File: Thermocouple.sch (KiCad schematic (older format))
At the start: 15 parts

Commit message: 5.3 Video 1/2 Associating and Placing the Relay Module
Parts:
- gave numbers to parts that had none: 13
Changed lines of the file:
@@
 Sheet 7 9
 Title ""
-Date "10 feb 2014"
+Date "19 feb 2014"
 Rev ""
 Comp ""
@@
 CS_N
 $Comp
-L LM324 U?
-U 1 1 52F15A12
+L LM324 U11
+U 2 1 52F15A12
 P 9000 2100
-F 0 "U?" H 9050 2300 60  0000 C CNN
+F 0 "U11" H 9050 2300 60  0000 C CNN
 F 1 "LM324" H 9150 1900 50  0000 C CNN
 F 2 "" H 9000 2100 60  0000 C CNN
 F 3 "" H 9000 2100 60  0000 C CNN
-	1    9000 2100
+	2    9000 2100
 	-1   0    0    -1
 $EndComp
 $Comp
-L LM324 U?
-U 1 1 52F15A1F
+L LM324 U11
+U 3 1 52F15A1F
 P 9000 4000
-F 0 "U?" H 9050 4200 60  0000 C CNN
+F 0 "U11" H 9050 4200 60  0000 C CNN
 F 1 "LM324" H 9150 3800 50  0000 C CNN
 F 2 "" H 9000 4000 60  0000 C CNN
 F 3 "" H 9000 4000 60  0000 C CNN
-	1    9000 4000
+	3    9000 4000
 	-1   0    0    1
 $EndComp
 $Comp
-L LM324 U?
+L LM324 U11
 U 1 1 52F15A25
 P 6700 2950
-F 0 "U?" H 6750 3150 60  0000 C CNN
+F 0 "U11" H 6750 3150 60  0000 C CNN
 F 1 "LM324" H 6850 2750 50  0000 C CNN
 F 2 "" H 6700 2950 60  0000 C CNN
@@
 $EndComp
 $Comp
-L LM324 U?
-U 1 1 52F15A2B
+L LM324 U7
+U 4 1 52F15A2B
 P 5550 5550
-F 0 "U?" H 5600 5750 60  0000 C CNN
+F 0 "U7" H 5600 5750 60  0000 C CNN
 F 1 "LM324" H 5700 5350 50  0000 C CNN
 F 2 "" H 5550 5550 60  0000 C CNN
 F 3 "" H 5550 5550 60  0000 C CNN
-	1    5550 5550
+	4    5550 5550
 	-1   0    0    -1
 $EndComp
 $Comp
-L R R?
+L R R21
 U 1 1 52F15A69
 P 5400 7350
-F 0 "R?" V 5480 7350 40  0000 C CNN
+F 0 "R21" V 5480 7350 40  0000 C CNN
 F 1 "R" V 5407 7351 40  0000 C CNN
 F 2 "" V 5330 7350 30  0000 C CNN
@@
 $EndComp
 $Comp
-L R R?
+L R R26
 U 1 1 52F15A76
 P 8050 2400
-F 0 "R?" V 8130 2400 40  0000 C CNN
+F 0 "R26" V 8130 2400 40  0000 C CNN
 F 1 "R" V 8057 2401 40  0000 C CNN
 F 2 "" V 7980 2400 30  0000 C CNN
@@
 $EndComp
 $Comp
-L R R?
+L R R28
 U 1 1 52F15A7C
 P 8050 3700
-F 0 "R?" V 8130 3700 40  0000 C CNN
+F 0 "R28" V 8130 3700 40  0000 C CNN
 F 1 "R" V 8057 3701 40  0000 C CNN
 F 2 "" V 7980 3700 30  0000 C CNN
@@
 $EndComp
 $Comp
-L R R?
+L R R27
 U 1 1 52F15A8C
 P 8050 3050
-F 0 "R?" V 8130 3050 40  0000 C CNN
+F 0 "R27" V 8130 3050 40  0000 C CNN
 F 1 "R" V 8057 3051 40  0000 C CNN
 F 2 "" V 7980 3050 30  0000 C CNN
@@
 $EndComp
 $Comp
-L R R?
+L R R24
 U 1 1 52F15A92
 P 7600 2100
-F 0 "R?" V 7680 2100 40  0000 C CNN
+F 0 "R24" V 7680 2100 40  0000 C CNN
 F 1 "R" V 7607 2101 40  0000 C CNN
 F 2 "" V 7530 2100 30  0000 C CNN
@@
 $EndComp
 $Comp
-L R R?
+L R R25
 U 1 1 52F15A98
 P 7600 4000
-F 0 "R?" V 7680 4000 40  0000 C CNN
+F 0 "R25" V 7680 4000 40  0000 C CNN
 F 1 "R" V 7607 4001 40  0000 C CNN
 F 2 "" V 7530 4000 30  0000 C CNN
@@
 $EndComp
 $Comp
-L R R?
+L R R22
 U 1 1 52F15B4F
 P 6700 2100
-F 0 "R?" V 6780 2100 40  0000 C CNN
+F 0 "R22" V 6780 2100 40  0000 C CNN
 F 1 "R" V 6707 2101 40  0000 C CNN
 F 2 "" V 6630 2100 30  0000 C CNN
@@
 $EndComp
 $Comp
-L R R?
+L R R23
 U 1 1 52F15B55
 P 6700 4000
-F 0 "R?" V 6780 4000 40  0000 C CNN
+F 0 "R23" V 6780 4000 40  0000 C CNN
 F 1 "R" V 6707 4001 40  0000 C CNN
 F 2 "" V 6630 4000 30  0000 C CNN
@@
 Instrumentation Amp
 $Comp
-L MCP3550-60-E/SN U?
+L MCP3550-60-E/SN U9
 U 1 1 52F18789
 P 3500 3100
-F 0 "U?" H 2950 3450 40  0000 C CNN
+F 0 "U9" H 2950 3450 40  0000 C CNN
 F 1 "MCP3550-60-E/SN" H 3200 3400 40  0000 C CNN
 F 2 "SO8" H 3300 3100 30  0000 C CIN
@@
 	2350 3200 3000 3200
 $Comp
-L +12V #PWR?
+L +12V #PWR039
 U 1 1 52F18A83
 P 9100 1500
-F 0 "#PWR?" H 9100 1450 20  0001 C CNN
+F 0 "#PWR039" H 9100 1450 20  0001 C CNN
 F 1 "+12V" H 9100 1600 30  0000 C CNN
 F 2 "" H 9100 1500 60  0000 C CNN
@@
 	9100 1500 9100 1700
 $Comp
-L +12V #PWR?
+L +12V #PWR040
 U 1 1 52F18AB9
 P 9100 4650
-F 0 "#PWR?" H 9100 4600 20  0001 C CNN
+F 0 "#PWR040" H 9100 4600 20  0001 C CNN
 F 1 "+12V" H 9100 4750 30  0000 C CNN
 F 2 "" H 9100 4650 60  0000 C CNN
@@
 	9100 4400 9100 4650
 $Comp
-L -12V #PWR?
+L -12V #PWR041
 U 1 1 52F18AF7
 P 9100 3500
-F 0 "#PWR?" H 9100 3630 20  0001 C CNN
+F 0 "#PWR041" H 9100 3630 20  0001 C CNN
 F 1 "-12V" H 9100 3600 30  0000 C CNN
 F 2 "" H 9100 3500 60  0000 C CNN
@@
 	9100 3500 9100 3600
 $Comp
-L -12V #PWR?
+L -12V #PWR042
 U 1 1 52F18B36
 P 9100 2600
-F 0 "#PWR?" H 9100 2730 20  0001 C CNN
+F 0 "#PWR042" H 9100 2730 20  0001 C CNN
 F 1 "-12V" H 9100 2700 30  0000 C CNN
 F 2 "" H 9100 2600 60  0000 C CNN
@@
 	9100 2500 9100 2600
 $Comp
-L -12V #PWR?
+L -12V #PWR043
 U 1 1 52F18BB0
 P 6800 2350
-F 0 "#PWR?" H 6800 2480 20  0001 C CNN
+F 0 "#PWR043" H 6800 2480 20  0001 C CNN
 F 1 "-12V" H 6800 2450 30  0000 C CNN
 F 2 "" H 6800 2350 60  0000 C CNN
@@
 $EndComp
 $Comp
-L +12V #PWR?
+L +12V #PWR044
 U 1 1 52F18BB6
 P 6800 3500
-F 0 "#PWR?" H 6800 3450 20  0001 C CNN
+F 0 "#PWR044" H 6800 3450 20  0001 C CNN
 F 1 "+12V" H 6800 3600 30  0000 C CNN
 F 2 "" H 6800 3500 60  0000 C CNN
@@
 	6200 2950 6200 2100
 $Comp
-L GND #PWR?
+L GND #PWR045
 U 1 1 52F18C2C
 P 6200 4200
-F 0 "#PWR?" H 6200 4200 30  0001 C CNN
+F 0 "#PWR045" H 6200 4200 30  0001 C CNN
 F 1 "GND" H 6200 4130 30  0001 C CNN
 F 2 "" H 6200 4200 60  0000 C CNN
@@
 	6200 4000 6200 4200
 $Comp
-L MCP3550-60-E/SN U?
+L MCP3550-60-E/SN U10
 U 1 1 52F18C65
 P 3500 5700
-F 0 "U?" H 2950 6050 40  0000 C CNN
+F 0 "U10" H 2950 6050 40  0000 C CNN
 F 1 "MCP3550-60-E/SN" H 3200 6000 40  0000 C CNN
 F 2 "SO8" H 3300 5700 30  0000 C CIN
@@
 Connection ~ 4850 5550
 $Comp
-L ZENER D?
+L ZENER D5
 U 1 1 52F18D23
 P 7350 5850
-F 0 "D?" H 7350 5950 50  0000 C CNN
+F 0 "D5" H 7350 5950 50  0000 C CNN
 F 1 "ZENER" H 7350 5750 40  0000 C CNN
 F 2 "" H 7350 5850 60  0000 C CNN
@@
 $EndComp
 $Comp
-L +12V #PWR?
+L +12V #PWR046
 U 1 1 52F18D32
 P 7350 5250
-F 0 "#PWR?" H 7350 5200 20  0001 C CNN
+F 0 "#PWR046" H 7350 5200 20  0001 C CNN
 F 1 "+12V" H 7350 5350 30  0000 C CNN
 F 2 "" H 7350 5250 60  0000 C CNN
@@
 	7350 5250 7350 5650
 $Comp
-L AGND #PWR?
+L AGND #PWR047
 U 1 1 52F18D78
 P 7350 6450
-F 0 "#PWR?" H 7350 6450 40  0001 C CNN
+F 0 "#PWR047" H 7350 6450 40  0001 C CNN
 F 1 "AGND" H 7350 6380 50  0000 C CNN
 F 2 "" H 7350 6450 60  0000 C CNN

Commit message: 5.4 Video 1/2 Associating and Placing the Thermocouple Module
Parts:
- removed D5: ZENER, symbol ZENER
- removed R21: R, symbol R
- removed U10, U9: MCP3550-60-E/SN, SO8, symbol MCP3550-60-E/SN
- removed U7: LM324, symbol LM324
- added C10, C5, C6, C7, C8, C9: C, ~, symbol C
- added P2: CONN_2, symbol CONN_2
- added P3: CONN_3X2, symbol CONN_3X2
- added R45, R46: R, symbol R
- added U10: MCP3901, symbol MCP3901
- added U11: LMT84, symbol LMT84
- U4: renamed from U11; value LM324 -> OPA4170
- renumbered R23 to R38, R22 to R39, R24 to R40, R25 to R41, R26 to R42, R28 to R43, R27 to R44
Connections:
- net labels added: +5V, REF+, REF-, ~CS, ~DR, ~RESET
- net labels removed: CS_N
- wire segments 39 -> 84
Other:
- note added: "16-24 bit ADC"
- note added: "Analog/TC Input"
- note removed: "16-24 bit ADC, TBD"
- note removed: "Fake Thermocouple"
- note removed: "Unused pins (at this time)\n"
- moved on the sheet: R38, R44

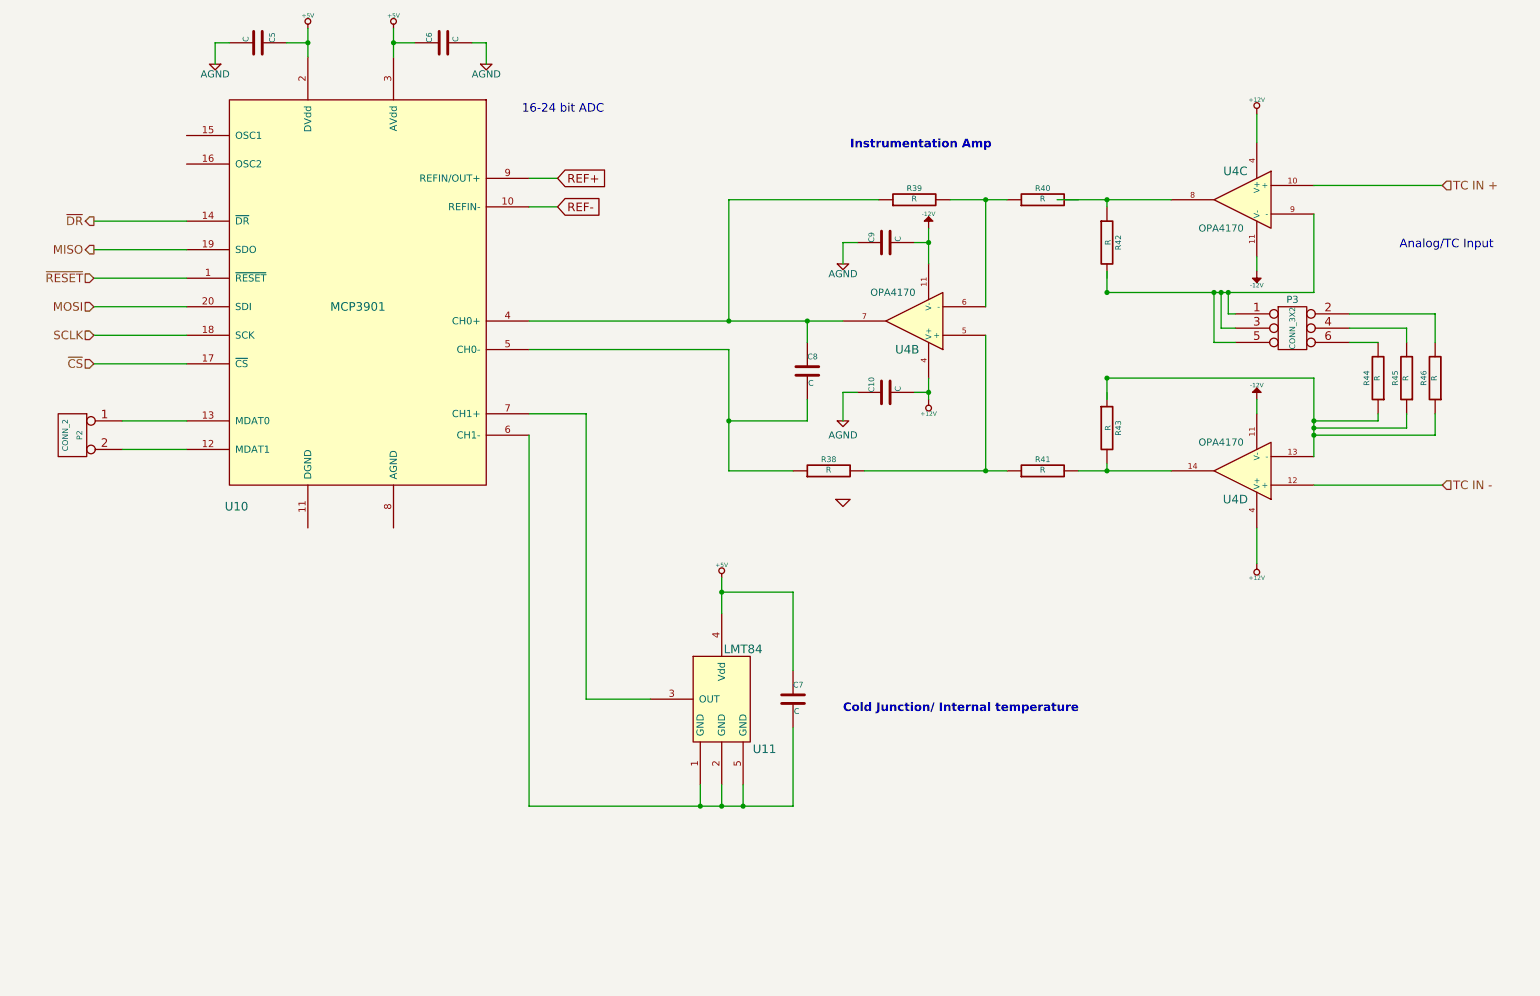
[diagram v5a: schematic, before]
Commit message: 5.4 Video 2/2 Associating and Placing the Thermocouple Module
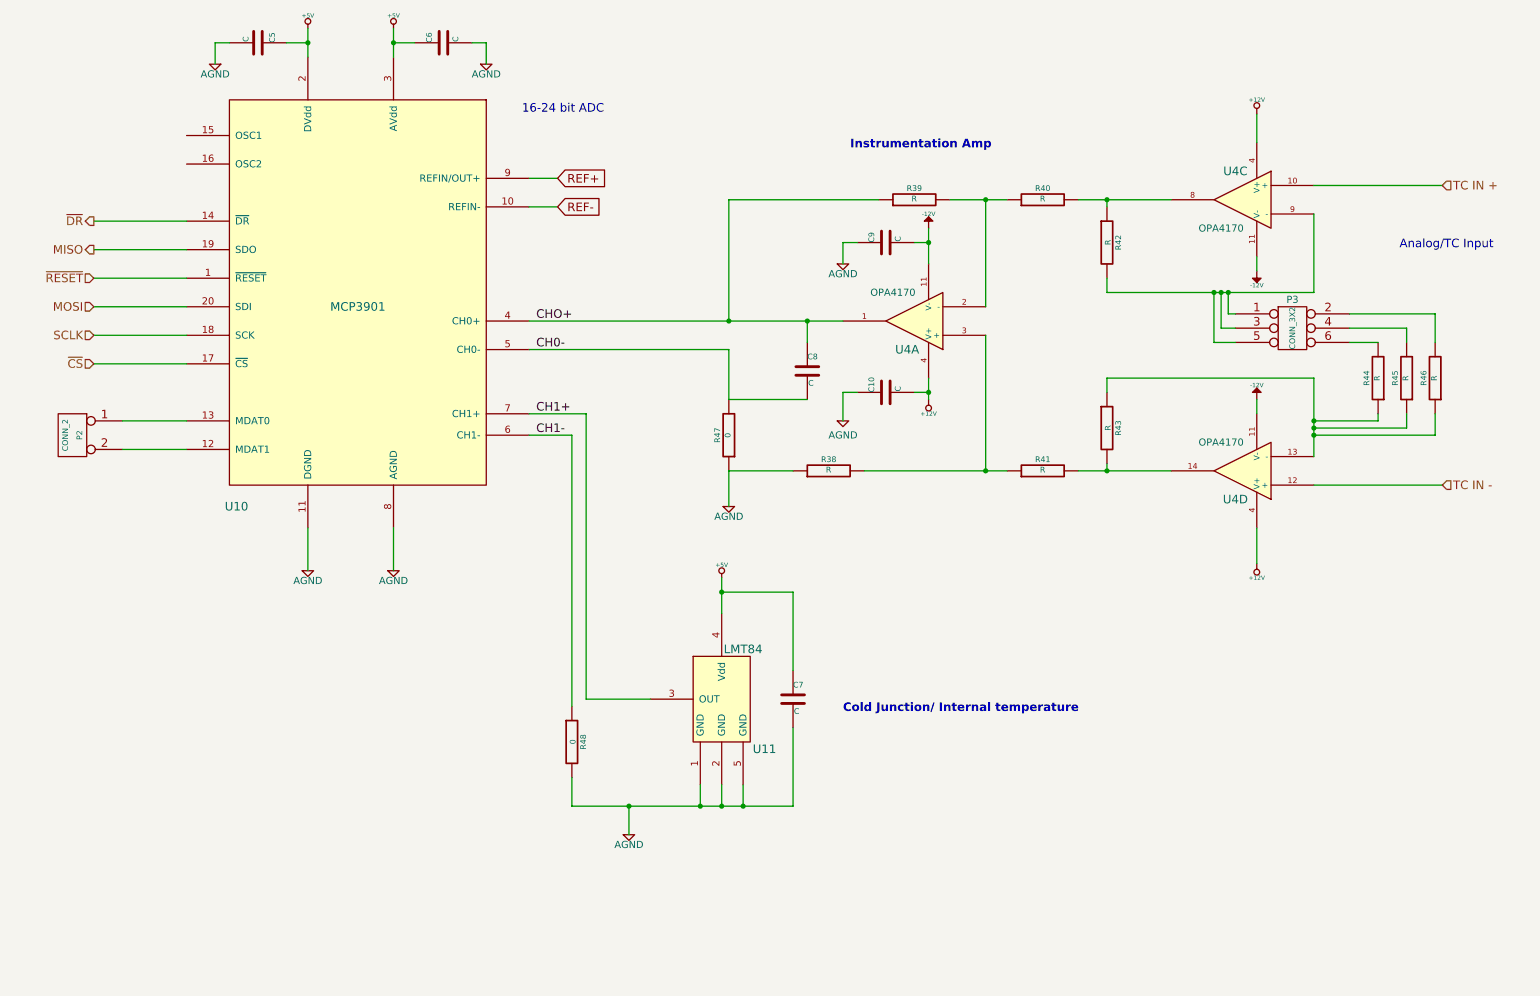
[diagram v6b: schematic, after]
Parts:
- added R47, R48: 0, symbol R
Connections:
- net labels added: CH0-, CH1+, CH1-, CHO+
- net labels removed: GND
- wire segments 84 -> 89
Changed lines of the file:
@@
 LIBS:BenchBudEE
 LIBS:BenchBudEE-cache
-EELAYER 27 0
+EELAYER 24 0
 EELAYER END
 $Descr A4 11693 8268
@@
 $Comp
 L LM324 U4
-U 2 1 52F15A25
+U 1 1 52F15A25
 P 6700 2950
 F 0 "U4" H 6750 3150 60  0000 C CNN
@@
 F 2 "" H 6700 2950 60  0000 C CNN
 F 3 "" H 6700 2950 60  0000 C CNN
-	2    6700 2950
+	1    6700 2950
 	-1   0    0    1
 $EndComp
@@
 	9500 4100 10400 4100
 Wire Wire Line
-	7700 2100 8500 2100
-Connection ~ 8050 2100
-Wire Wire Line
-	8050 2600 8050 2750
-Wire Wire Line
-	8050 3350 8050 3500
+	7850 2100 8500 2100
 Wire Wire Line
 	7850 4000 8500 4000
@@
 Wire Wire Line
 	9500 3350 8050 3350
-Connection ~ 8050 3350
 Wire Wire Line
 	7200 2100 7200 2850
@@
 Instrumentation Amp
 $Comp
-L +12V #PWR52
+L +12V #PWR041
 U 1 1 52F18A83
 P 9100 1500
-F 0 "#PWR52" H 9100 1450 20  0001 C CNN
+F 0 "#PWR041" H 9100 1450 20  0001 C CNN
 F 1 "+12V" H 9100 1600 30  0000 C CNN
 F 2 "" H 9100 1500 60  0000 C CNN
@@
 	9100 1500 9100 1700
 $Comp
-L +12V #PWR55
+L +12V #PWR042
 U 1 1 52F18AB9
 P 9100 4650
-F 0 "#PWR55" H 9100 4600 20  0001 C CNN
+F 0 "#PWR042" H 9100 4600 20  0001 C CNN
 F 1 "+12V" H 9100 4750 30  0000 C CNN
 F 2 "" H 9100 4650 60  0000 C CNN
@@
 	9100 4400 9100 4650
 $Comp
-L -12V #PWR54
+L -12V #PWR043
 U 1 1 52F18AF7
 P 9100 3500
-F 0 "#PWR54" H 9100 3630 20  0001 C CNN
+F 0 "#PWR043" H 9100 3630 20  0001 C CNN
 F 1 "-12V" H 9100 3600 30  0000 C CNN
 F 2 "" H 9100 3500 60  0000 C CNN
@@
 	9100 3500 9100 3600
 $Comp
-L -12V #PWR53
+L -12V #PWR044
 U 1 1 52F18B36
 P 9100 2600
-F 0 "#PWR53" H 9100 2730 20  0001 C CNN
+F 0 "#PWR044" H 9100 2730 20  0001 C CNN
 F 1 "-12V" H 9100 2700 30  0000 C CNN
 F 2 "" H 9100 2600 60  0000 C CNN
@@
 Wire Wire Line
 	8050 2750 9500 2750
-Connection ~ 8050 2750
 Wire Wire Line
 	9100 2500 9100 2600
 $Comp
-L -12V #PWR50
+L -12V #PWR045
 U 1 1 52F18BB0
 P 6800 2300
-F 0 "#PWR50" H 6800 2430 20  0001 C CNN
+F 0 "#PWR045" H 6800 2430 20  0001 C CNN
 F 1 "-12V" H 6800 2400 30  0000 C CNN
 F 2 "" H 6800 2300 60  0000 C CNN
@@
 $EndComp
 $Comp
-L +12V #PWR51
+L +12V #PWR046
 U 1 1 52F18BB6
 P 6800 3500
-F 0 "#PWR51" H 6800 3450 20  0001 C CNN
+F 0 "#PWR046" H 6800 3450 20  0001 C CNN
 F 1 "+12V" H 6800 3600 30  0000 C CNN
 F 2 "" H 6800 3500 60  0000 C CNN
@@
 Wire Wire Line
 	6800 2300 6800 2550
-$Comp
-L GND #PWR49
-U 1 1 52F18C2C
-P 6200 4200
-F 0 "#PWR49" H 6200 4200 30  0001 C CNN
-F 1 "GND" H 6200 4130 30  0001 C CNN
-F 2 "" H 6200 4200 60  0000 C CNN
-F 3 "" H 6200 4200 60  0000 C CNN
-	1    6200 4200
-	1    0    0    -1
-$EndComp
 Text Notes 6200 5700 0    60   ~ 12
 Cold Junction/ Internal temperature
@@
 Wire Wire Line
 	4000 3150 5400 3150
-Wire Wire Line
-	5400 3150 5400 4000
 Connection ~ 5400 2950
 $Comp
@@
 	5950 2950 5950 3100
 Connection ~ 5950 2950
-Wire Wire Line
-	5950 3500 5950 3650
-Wire Wire Line
-	5950 3650 5400 3650
-Connection ~ 5400 3650
 $Comp
 L C C7
@@
 	4400 3600 4000 3600
 Wire Wire Line
-	4000 3750 4000 6350
-Wire Wire Line
-	4000 6350 5850 6350
+	4300 6350 5850 6350
 Wire Wire Line
 	5500 6350 5500 6200
@@
 Connection ~ 5200 6350
 $Comp
-L +5V #PWR46
+L +5V #PWR047
 U 1 1 5306CFFA
 P 5350 4750
-F 0 "#PWR46" H 5350 4840 20  0001 C CNN
+F 0 "#PWR047" H 5350 4840 20  0001 C CNN
 F 1 "+5V" H 5350 4840 30  0000 C CNN
 F 2 "" H 5350 4750 60  0000 C CNN
@@
 	6800 3450 6700 3450
 $Comp
-L AGND #PWR48
+L AGND #PWR048
 U 1 1 5306D278
 P 6200 3650
-F 0 "#PWR48" H 6200 3650 40  0001 C CNN
+F 0 "#PWR048" H 6200 3650 40  0001 C CNN
 F 1 "AGND" H 6200 3550 50  0000 C CNN
 F 2 "" H 6200 3650 60  0000 C CNN
@@
 $EndComp
 $Comp
-L AGND #PWR47
+L AGND #PWR049
 U 1 1 5306D2E6
 P 6200 2550
-F 0 "#PWR47" H 6200 2550 40  0001 C CNN
+F 0 "#PWR049" H 6200 2550 40  0001 C CNN
 F 1 "AGND" H 6200 2480 50  0000 C CNN
 F 2 "" H 6200 2550 60  0000 C CNN
@@
 	6200 3450 6200 3650
 $Comp
-L +5V #PWR44
+L +5V #PWR050
 U 1 1 5306D522
 P 3050 900
-F 0 "#PWR44" H 3050 990 20  0001 C CNN
+F 0 "#PWR050" H 3050 990 20  0001 C CNN
 F 1 "+5V" H 3050 990 30  0000 C CNN
 F 2 "" H 3050 900 60  0000 C CNN
@@
 Connection ~ 3050 1000
 $Comp
-L AGND #PWR45
+L AGND #PWR051
 U 1 1 5306D6F7
 P 3700 1150
-F 0 "#PWR45" H 3700 1150 40  0001 C CNN
+F 0 "#PWR051" H 3700 1150 40  0001 C CNN
 F 1 "AGND" H 3700 1080 50  0000 C CNN
 F 2 "" H 3700 1150 60  0000 C CNN
@@
 	3700 1000 3700 1150
 $Comp
-L +5V #PWR43
+L +5V #PWR052
 U 1 1 5306D76D
 P 2450 900
-F 0 "#PWR43" H 2450 990 20  0001 C CNN
+F 0 "#PWR052" H 2450 990 20  0001 C CNN
 F 1 "+5V" H 2450 990 30  0000 C CNN
 F 2 "" H 2450 900 60  0000 C CNN
@@
 Connection ~ 2450 1000
 $Comp
-L AGND #PWR42
+L AGND #PWR053
 U 1 1 5306D77C
 P 1800 1150
-F 0 "#PWR42" H 1800 1150 40  0001 C CNN
+F 0 "#PWR053" H 1800 1150 40  0001 C CNN
 F 1 "AGND" H 1800 1080 50  0000 C CNN
 F 2 "" H 1800 1150 60  0000 C CNN
@@
 Wire Wire Line
 	1150 3850 1600 3850
+Wire Wire Line
+	4000 3750 4300 3750
+Text Label 4050 2950 0    60   ~ 0
+CHO+
+Text Label 4050 3150 0    60   ~ 0
+CH0-
+Text Label 4050 3600 0    60   ~ 0
+CH1+
+Text Label 4050 3750 0    60   ~ 0
+CH1-
+$Comp
+L AGND #PWR054
+U 1 1 5307B274
+P 3050 4700
+F 0 "#PWR054" H 3050 4700 40  0001 C CNN
+F 1 "AGND" H 3050 4630 50  0000 C CNN
+F 2 "" H 3050 4700 60  0000 C CNN
+F 3 "" H 3050 4700 60  0000 C CNN
+	1    3050 4700
+	1    0    0    -1
+$EndComp
+$Comp
+L AGND #PWR055
+U 1 1 5307B290
+P 2450 4700
+F 0 "#PWR055" H 2450 4700 40  0001 C CNN
+F 1 "AGND" H 2450 4630 50  0000 C CNN
+F 2 "" H 2450 4700 60  0000 C CNN
+F 3 "" H 2450 4700 60  0000 C CNN
+	1    2450 4700
+	1    0    0    -1
+$EndComp
+Wire Wire Line
+	3050 4400 3050 4700
+Wire Wire Line
+	2450 4700 2450 4400
+$Comp
+L R R47
+U 1 1 5307B3DA
+P 5400 3750
+F 0 "R47" V 5480 3750 40  0000 C CNN
+F 1 "0" V 5407 3751 40  0000 C CNN
+F 2 "" V 5330 3750 30  0000 C CNN
+F 3 "" H 5400 3750 30  0000 C CNN
+	1    5400 3750
+	-1   0    0    1
+$EndComp
+Wire Wire Line
+	5950 3500 5400 3500
+Wire Wire Line
+	5400 3500 5400 3150
+Wire Wire Line
+	5400 4000 5400 4250
+$Comp
+L AGND #PWR056
+U 1 1 5307B5BC
+P 4700 6550
+F 0 "#PWR056" H 4700 6550 40  0001 C CNN
+F 1 "AGND" H 4700 6480 50  0000 C CNN
+F 2 "" H 4700 6550 60  0000 C CNN
+F 3 "" H 4700 6550 60  0000 C CNN
+	1    4700 6550
+	1    0    0    -1
+$EndComp
+Wire Wire Line
+	4700 6350 4700 6550
+Connection ~ 4700 6350
+$Comp
+L R R48
+U 1 1 5307B639
+P 4300 5900
+F 0 "R48" V 4380 5900 40  0000 C CNN
+F 1 "0" V 4307 5901 40  0000 C CNN
+F 2 "" V 4230 5900 30  0000 C CNN
+F 3 "" H 4300 5900 30  0000 C CNN
+	1    4300 5900
+	1    0    0    -1
+$EndComp
+Wire Wire Line
+	4300 6350 4300 6150
+Wire Wire Line
+	4300 3750 4300 5650
+$Comp
+L AGND #PWR057
+U 1 1 5307B7A7
+P 5400 4250
+F 0 "#PWR057" H 5400 4250 40  0001 C CNN
+F 1 "AGND" H 5400 4180 50  0000 C CNN
+F 2 "" H 5400 4250 60  0000 C CNN
+F 3 "" H 5400 4250 60  0000 C CNN
+	1    5400 4250
+	1    0    0    -1
+$EndComp
+Wire Wire Line
+	8050 3350 8050 3450
+Wire Wire Line
+	8050 2750 8050 2650
+Connection ~ 8050 2100
 $EndSCHEMATC
